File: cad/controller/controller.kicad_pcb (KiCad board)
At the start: 2 copper layers, 95 x 80 mm, 105 parts, among them J1 RJ45_jack_POE, J2 Barrel_Jack, J3 Conn_02x03_Odd_Even, J4 Conn_01x02, J5 Conn_01x04, J6 Conn_01x05, J7 6P6C, SW1 SW_Push, SW2 SW_Push, U1 NCP1117-5.0_SOT223, U2 NCP1117-3.3_SOT223, U3 CAT811STBI-GT3, U4 W5500, U5 ATmega328-PU, U6 PCA9517A, U7 TXB0104D, Y1 25MHz, Y2 18MHz

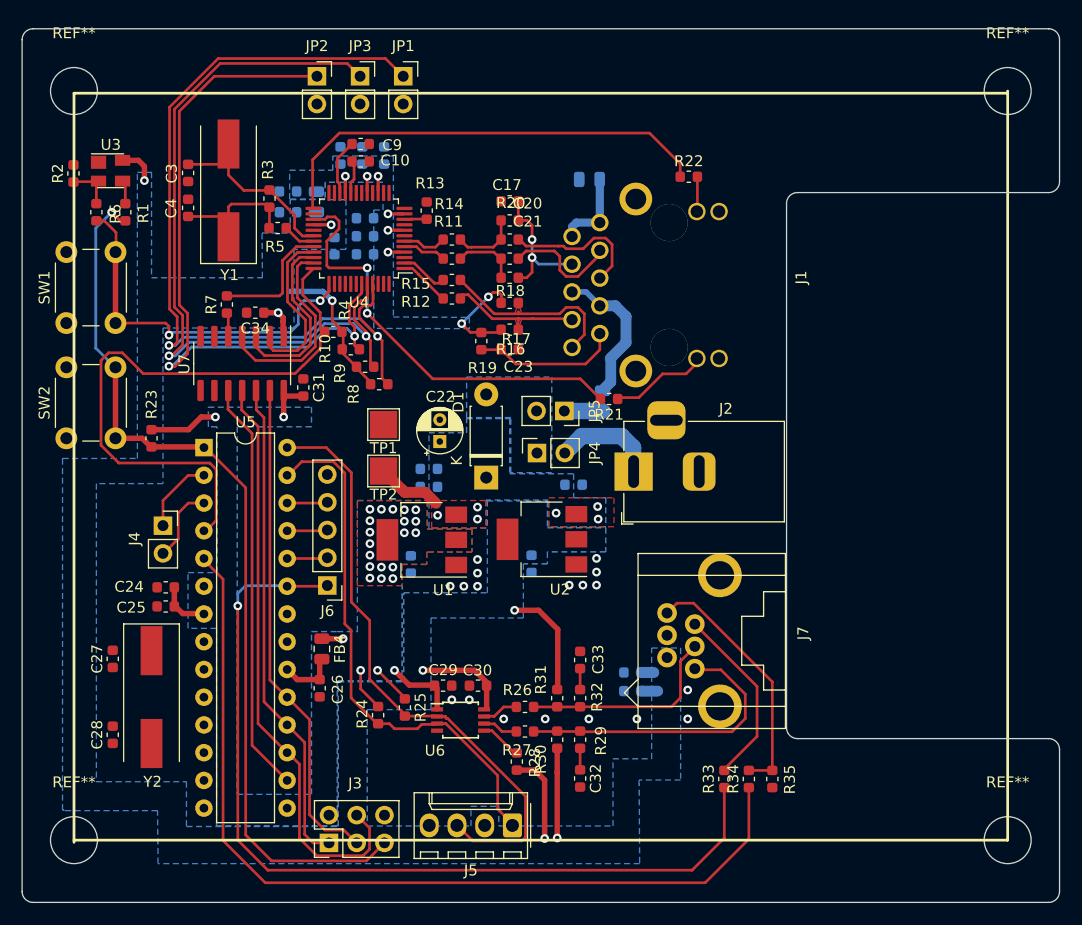
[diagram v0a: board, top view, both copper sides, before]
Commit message: Finished layout of controller (need to fix silkscreen and generate gerbers)
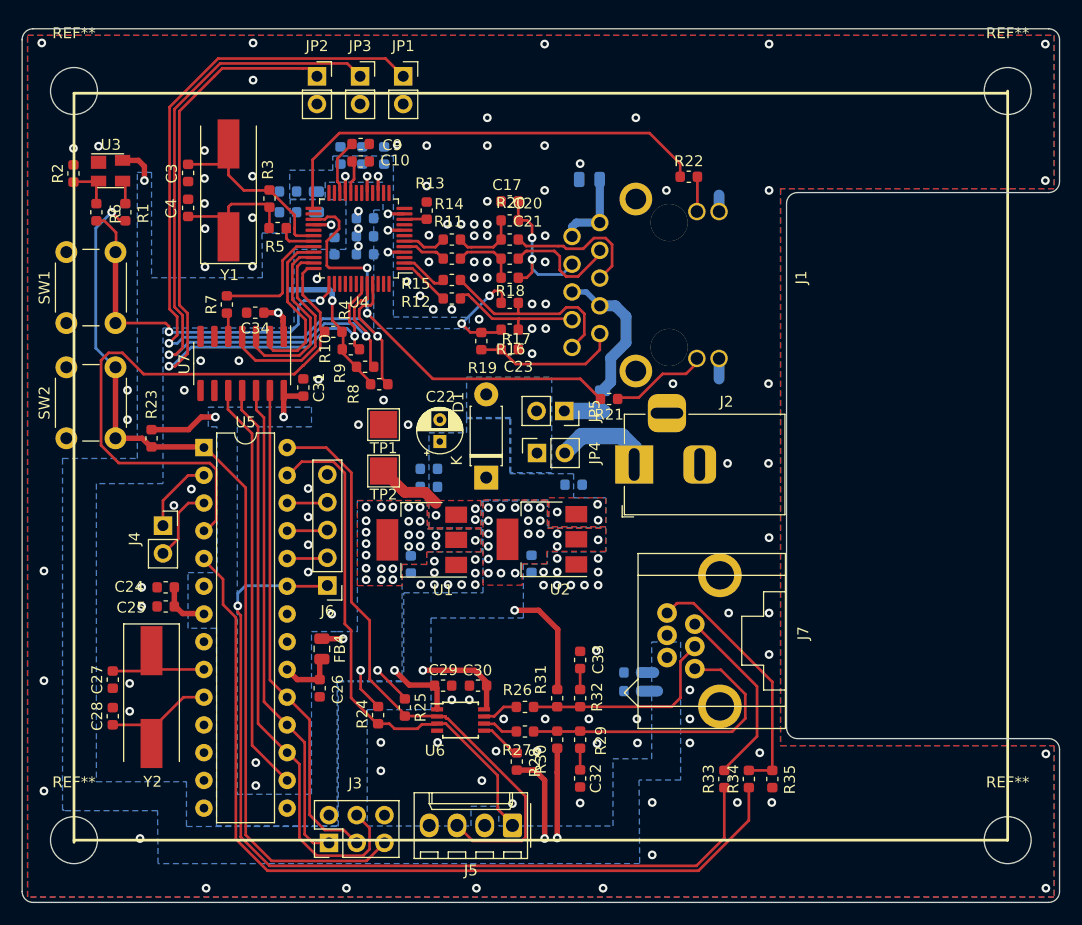
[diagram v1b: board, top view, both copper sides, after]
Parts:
- J2: value Barrel_Jack -> Barrel_Jack_Switch
- moved C27 1.90 mm to (103.5, 103.9)
- moved C28 1.70 mm to (103.5, 107.2)
- moved J2 0.65 mm to (151.3, 84.2)
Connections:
- J2 pad 3: (no net) -> GND
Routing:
- net Net-(C28-Pad1): track 0.00 -> 7.91 mm
- net Net-(C27-Pad2): track 0.00 -> 6.81 mm
- net GND: track 0.00 -> 3.39 mm, vias 11 -> 141
- net /MCU/INT_SPARE: track 82.7 -> 80.0 mm
- net /3V3_ANA: track 17.4 -> 18.6 mm
- net Net-(C17-Pad1): track 12.9 -> 14.1 mm
- net Net-(JP2-Pad1): track 64.0 -> 64.9 mm
- net Net-(R5-Pad2): track 2.71 -> 3.39 mm
- net /MCU/ADC_0: track 82.4 -> 81.7 mm
- net /PIN_12V_JACK: track 9.59 -> 8.93 mm
- net Net-(JP1-Pad1): track 78.7 -> 78.1 mm
- net 3V3: track 60.0 -> 60.5 mm, vias 8 -> 27
- net 5V0: vias 25 -> 30
- net (no net): vias 7 -> 0
- added copper zone on F.Cu, net 3V3
- added copper zone on B.Cu, net GND
- added copper zone on F.Cu, net GND
- removed copper zone on F.Cu, net Net-(J1-Pad10)
- removed copper zone on F.Cu, net Net-(J1-Pad8)

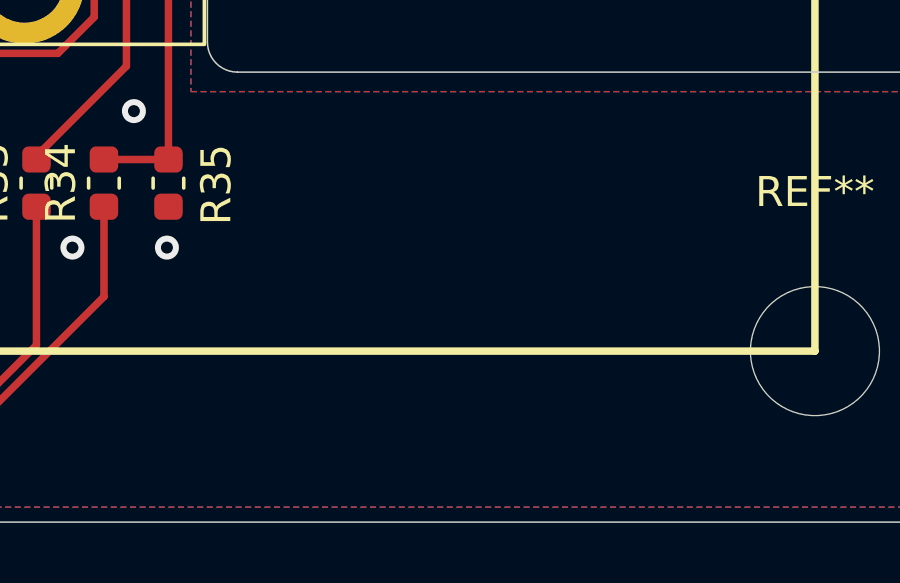
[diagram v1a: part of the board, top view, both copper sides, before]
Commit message: Finished routing wind sensor(s) board
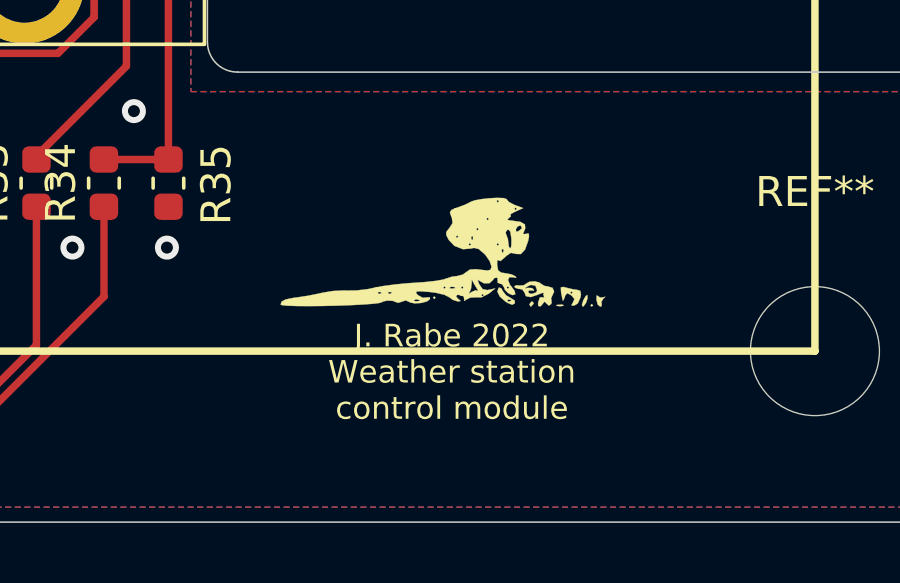
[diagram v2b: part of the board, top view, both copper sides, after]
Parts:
- added G***: LOGO, custom:logo_JR_3, F.Cu at (173.7, 115.0)
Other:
- board text added: "J. Rabe 2022 Weather station control module"

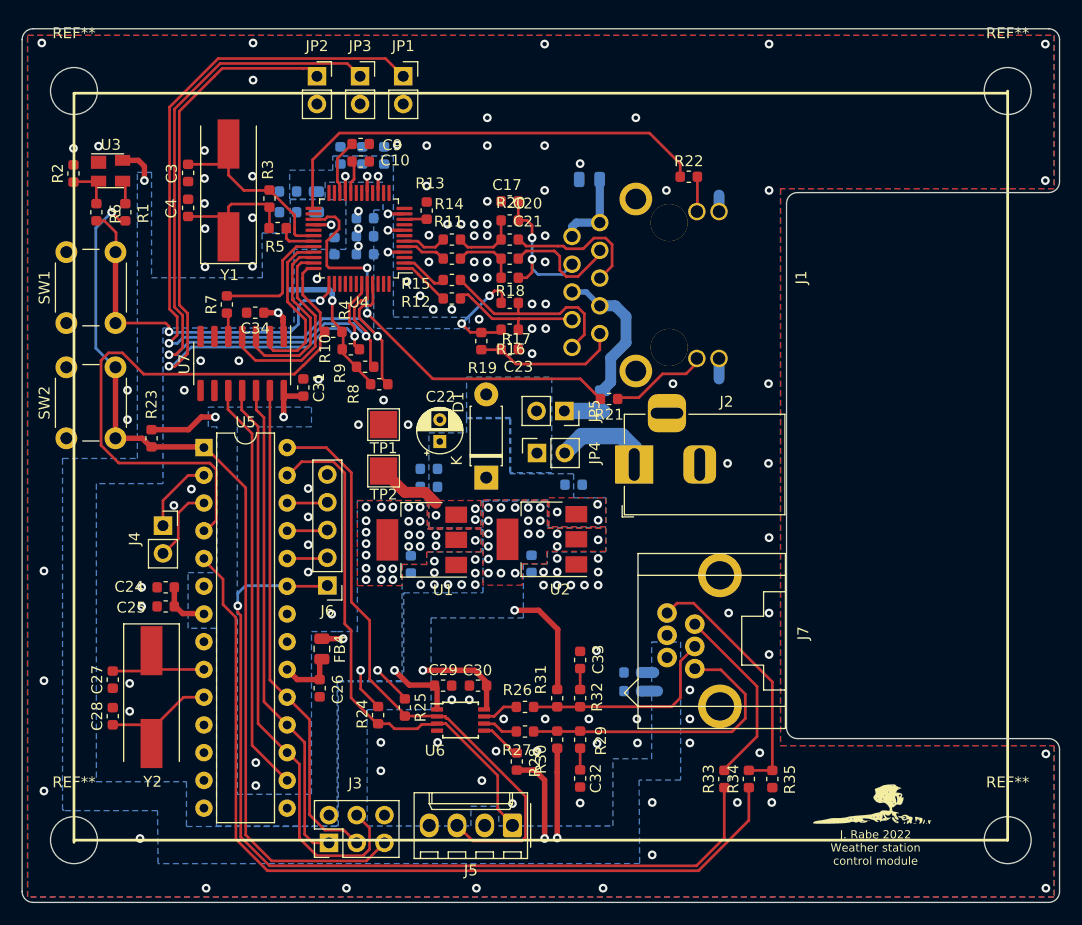
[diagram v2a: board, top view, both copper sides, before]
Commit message: Finished PCB layout
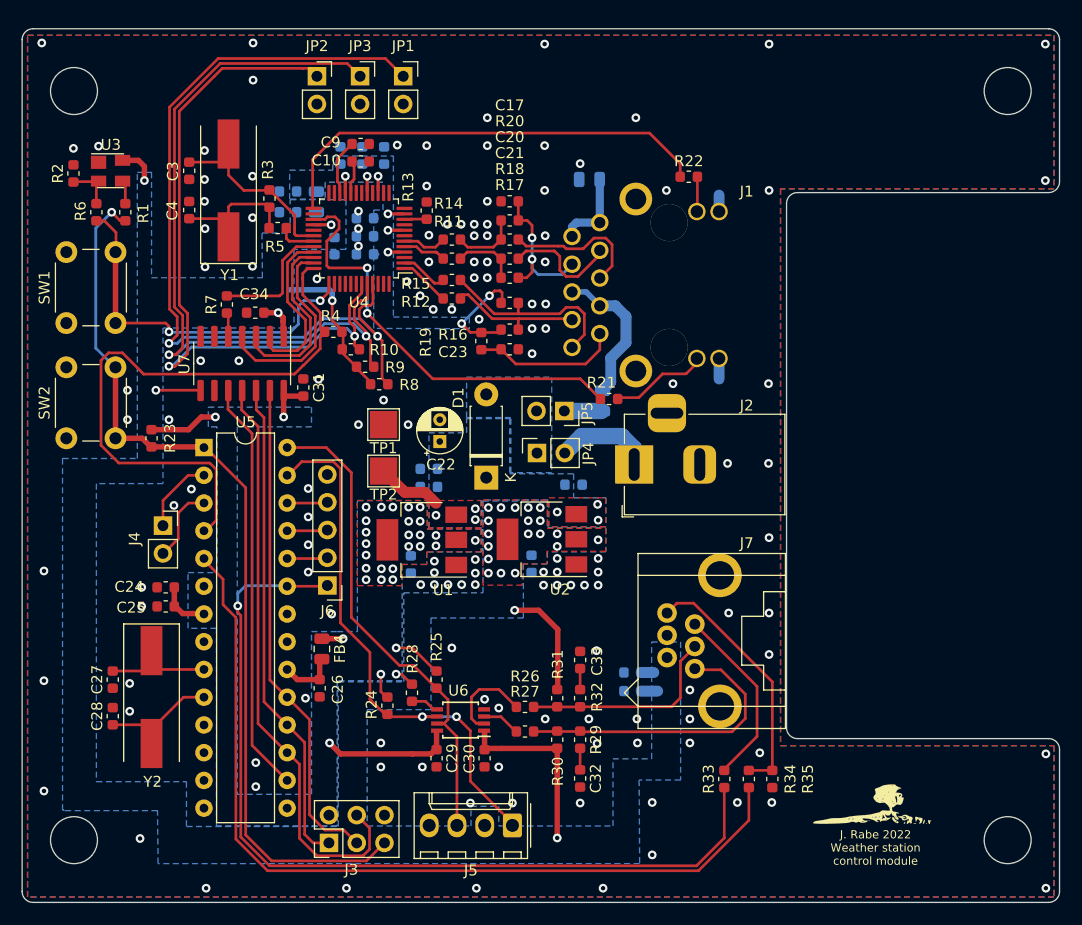
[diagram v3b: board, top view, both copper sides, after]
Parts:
- moved R28 11.5 mm to (130.9, 105.1), turned to 270 degrees
- moved C29 6.68 mm to (133.2, 111.1), turned to 270 degrees
- moved C30 6.68 mm to (137.6, 111.1), turned to 270 degrees
- moved R25 3.86 mm to (133.2, 103.9)
- moved R24 1.21 mm to (128.7, 106.3)
- moved C3 0.22 mm to (110.5, 57.3)
- moved C4 0.22 mm to (110.5, 60.9)
- turned U6 to 180 degrees
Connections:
- R28 pad 1: 3V3 -> 5V0
- U6 pad 1: 5V0 -> 3V3
- U6 pad 2: /MCU/SCL -> Net-(R26-Pad2)
- U6 pad 3: /MCU/SDA -> Net-(R27-Pad2)
- U6 pad 6: Net-(R27-Pad2) -> /MCU/SDA
- U6 pad 7: Net-(R26-Pad2) -> /MCU/SCL
- U6 pad 8: 3V3 -> 5V0
- U7 pad 8: GND -> 3V3
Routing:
- net /MCU/SCL: track 55.7 -> 44.8 mm
- net 5V0: track 31.3 -> 37.7 mm, vias 30 -> 31
- net Net-(R26-Pad2): track 3.31 -> 8.11 mm
- net 3V3: track 60.5 -> 56.2 mm, vias 27 -> 26
- net Net-(R28-Pad2): track 3.81 -> 2.25 mm
- net /MCU/SDA: track 48.5 -> 49.0 mm, vias 0 -> 2
